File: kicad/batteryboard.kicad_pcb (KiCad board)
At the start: 2 copper layers, 41.9 x 72.4 mm, 19 parts, among them U1 PANSTAMP_02, U3 DHT22, U4 MAX1724

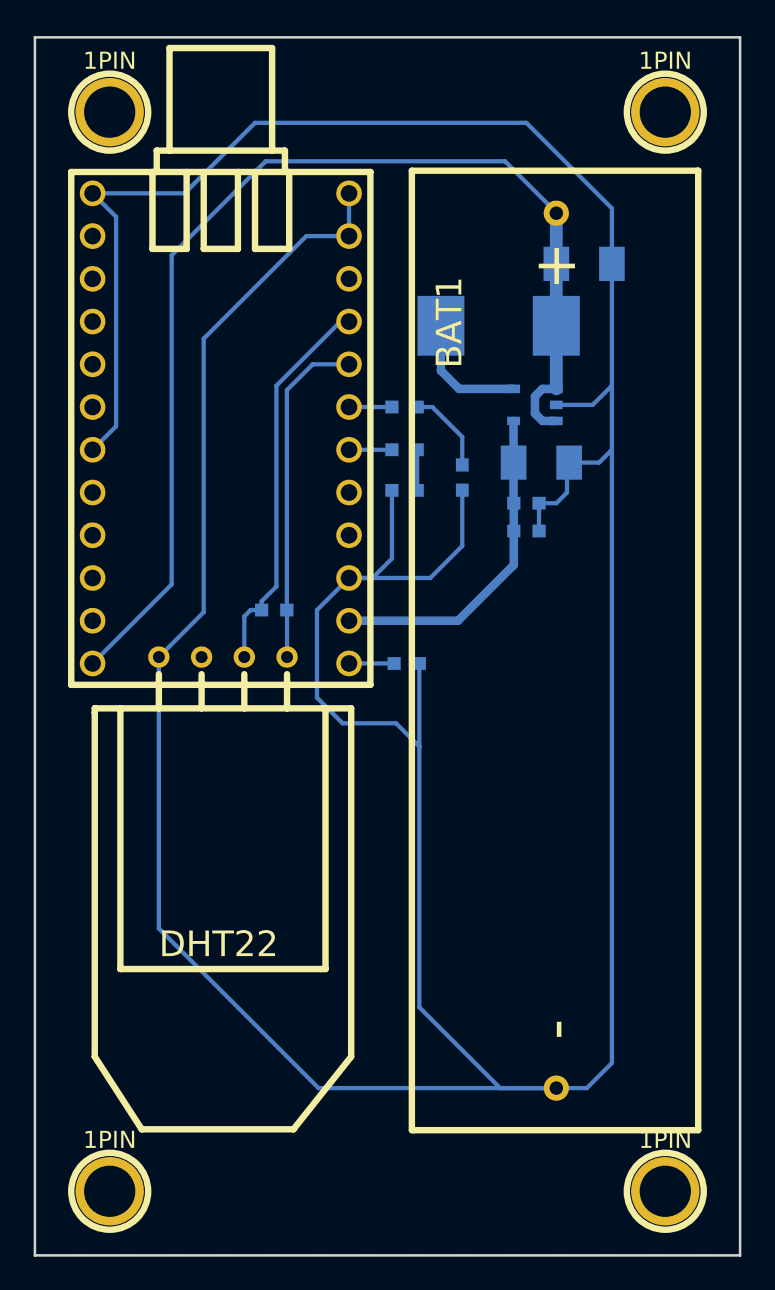
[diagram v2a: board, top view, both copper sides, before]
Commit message: add text
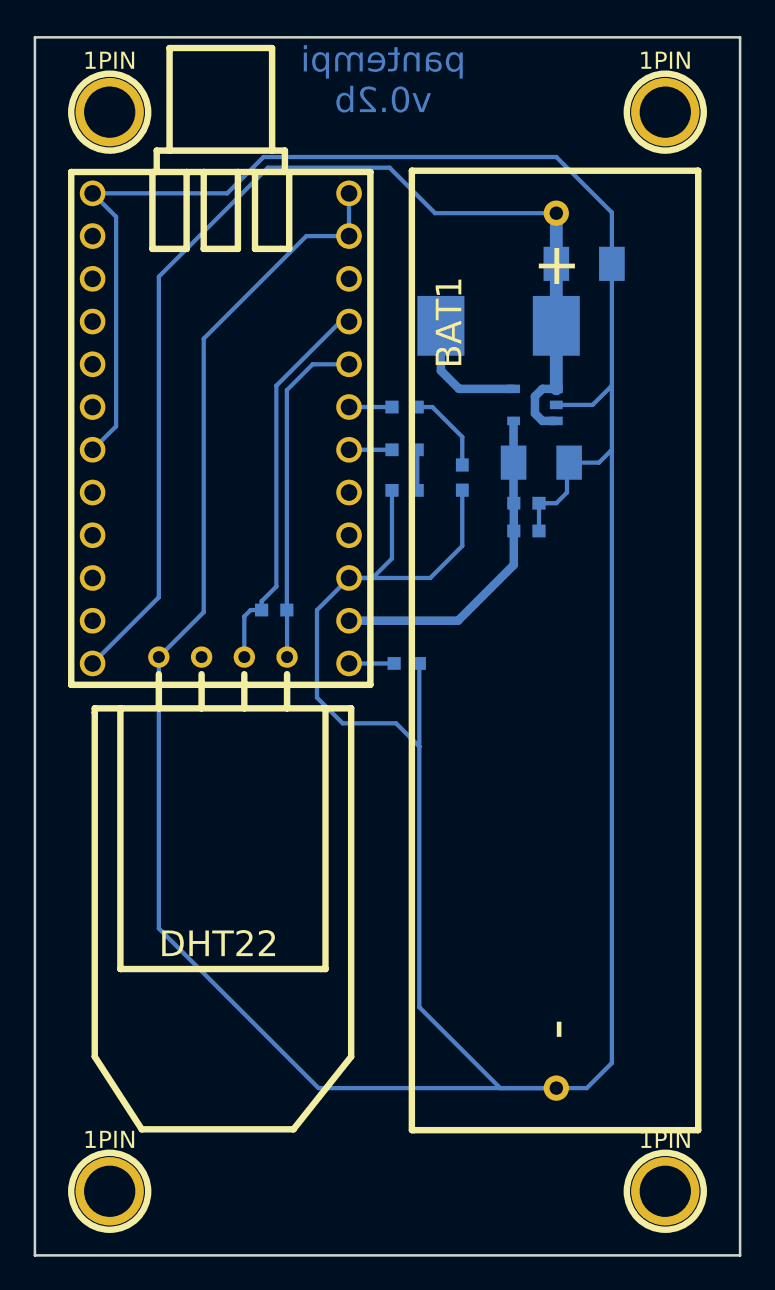
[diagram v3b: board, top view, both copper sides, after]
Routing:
- net GND: track 258.9 -> 257.1 mm
- net /BATTERY: track 67.0 -> 66.4 mm
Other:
- board text added: "pantempi v0.2b"
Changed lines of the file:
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@@
     (area 159.944999 68.504999 202.005001 141.045001)
     (thickness 1.6)
-    (drawings 4)
+    (drawings 5)
     (tracks 89)
     (zones 0)
@@
     )
   )
+  (gr_text "pantempi\nv0.2b" (at 180.721 71.12) (layer B.Cu)
+    (effects (font (size 1.5 1.5) (thickness 0.3)) (justify mirror))
+  )
   (gr_line (start 160.02 140.97) (end 160.02 68.58) (angle 90) (layer Edge.Cuts) (width 0.15))
   (gr_line (start 201.93 140.97) (end 160.02 140.97) (angle 90) (layer Edge.Cuts) (width 0.15))
@@
   (segment (start 188.468 96.2533) (end 188.4807 96.266) (width 0.508) (layer B.Cu) (net 1))
   (segment (start 188.468 91.3765) (end 188.468 93.853) (width 0.508) (layer B.Cu) (net 1))
-  (segment (start 173.4947 102.616) (end 173.4947 102.0953) (width 0.254) (layer B.Cu) (net 2) (status 400000))
-  (segment (start 178.181 85.471) (end 178.689 85.471) (width 0.254) (layer B.Cu) (net 2) (status C00000))
-  (segment (start 174.371 89.281) (end 178.181 85.471) (width 0.254) (layer B.Cu) (net 2) (status 800000))
+  (segment (start 173.4947 102.616) (end 173.4947 102.0953) (width 0.254) (layer B.Cu) (net 2))
+  (segment (start 178.181 85.471) (end 178.689 85.471) (width 0.254) (layer B.Cu) (net 2))
+  (segment (start 174.371 89.281) (end 178.181 85.471) (width 0.254) (layer B.Cu) (net 2))
   (segment (start 174.371 101.219) (end 174.371 89.281) (width 0.254) (layer B.Cu) (net 2))
   (segment (start 173.4947 102.0953) (end 174.371 101.219) (width 0.254) (layer B.Cu) (net 2))
-  (segment (start 172.466 105.41) (end 172.466 102.997) (width 0.254) (layer B.Cu) (net 2) (status 400000))
-  (segment (start 172.847 102.616) (end 173.4947 102.616) (width 0.254) (layer B.Cu) (net 2) (status 800000))
+  (segment (start 172.466 105.41) (end 172.466 102.997) (width 0.254) (layer B.Cu) (net 2))
+  (segment (start 172.847 102.616) (end 173.4947 102.616) (width 0.254) (layer B.Cu) (net 2))
   (segment (start 172.466 102.997) (end 172.847 102.616) (width 0.254) (layer B.Cu) (net 2))
-  (segment (start 174.9933 102.616) (end 174.9933 89.5477) (width 0.254) (layer B.Cu) (net 3) (status 400000))
-  (segment (start 176.53 88.011) (end 178.689 88.011) (width 0.254) (layer B.Cu) (net 3) (status 800000))
+  (segment (start 174.9933 102.616) (end 174.9933 89.5477) (width 0.254) (layer B.Cu) (net 3))
+  (segment (start 176.53 88.011) (end 178.689 88.011) (width 0.254) (layer B.Cu) (net 3))
   (segment (start 174.9933 89.5477) (end 176.53 88.011) (width 0.254) (layer B.Cu) (net 3))
-  (segment (start 175.006 105.41) (end 175.006 102.6287) (width 0.254) (layer B.Cu) (net 3) (status C00000))
-  (segment (start 175.006 102.6287) (end 174.9933 102.616) (width 0.254) (layer B.Cu) (net 3) (status C00000))
-  (segment (start 191.008 79.02956) (end 191.008 78.994) (width 0.254) (layer B.Cu) (net 4) (status C00000))
-  (segment (start 168.148 101.092) (end 163.449 105.791) (width 0.254) (layer B.Cu) (net 4) (status 800000))
-  (segment (start 168.148 81.534) (end 168.148 101.092) (width 0.254) (layer B.Cu) (net 4))
-  (segment (start 173.736 75.946) (end 168.148 81.534) (width 0.254) (layer B.Cu) (net 4))
-  (segment (start 187.96 75.946) (end 173.736 75.946) (width 0.254) (layer B.Cu) (net 4))
-  (segment (start 191.008 78.994) (end 187.96 75.946) (width 0.254) (layer B.Cu) (net 4) (status 400000))
+  (segment (start 175.006 105.41) (end 175.006 102.6287) (width 0.254) (layer B.Cu) (net 3))
+  (segment (start 175.006 102.6287) (end 174.9933 102.616) (width 0.254) (layer B.Cu) (net 3))
+  (segment (start 191.008 79.02956) (end 183.80456 79.02956) (width 0.254) (layer B.Cu) (net 4) (status 400000))
+  (segment (start 167.386 101.854) (end 163.449 105.791) (width 0.254) (layer B.Cu) (net 4) (status 800000))
+  (segment (start 167.386 82.804) (end 167.386 101.854) (width 0.254) (layer B.Cu) (net 4))
+  (segment (start 173.863 76.327) (end 167.386 82.804) (width 0.254) (layer B.Cu) (net 4))
+  (segment (start 181.102 76.327) (end 173.863 76.327) (width 0.254) (layer B.Cu) (net 4))
+  (segment (start 183.80456 79.02956) (end 181.102 76.327) (width 0.254) (layer B.Cu) (net 4))
   (segment (start 191.008 89.4715) (end 190.1825 89.4715) (width 0.508) (layer B.Cu) (net 4))
   (segment (start 190.1825 91.3765) (end 191.008 91.3765) (width 0.508) (layer B.Cu) (net 4))
@@
   (segment (start 181.2417 90.551) (end 178.689 90.551) (width 0.254) (layer B.Cu) (net 6))
   (segment (start 181.3687 105.791) (end 178.689 105.791) (width 0.254) (layer B.Cu) (net 7))
-  (segment (start 178.689 80.391) (end 176.149 80.391) (width 0.254) (layer B.Cu) (net 8) (status 400000))
-  (segment (start 170.053 102.743) (end 167.386 105.41) (width 0.254) (layer B.Cu) (net 8) (status 800000))
+  (segment (start 163.449 77.851) (end 171.45 77.851) (width 0.254) (layer B.Cu) (net 8) (status 400000))
+  (segment (start 194.31 78.994) (end 194.31 82.042) (width 0.254) (layer B.Cu) (net 8) (status 800000))
+  (segment (start 191.008 75.692) (end 194.31 78.994) (width 0.254) (layer B.Cu) (net 8))
+  (segment (start 173.609 75.692) (end 191.008 75.692) (width 0.254) (layer B.Cu) (net 8))
+  (segment (start 171.45 77.851) (end 173.609 75.692) (width 0.254) (layer B.Cu) (net 8))
+  (segment (start 178.689 80.391) (end 176.149 80.391) (width 0.254) (layer B.Cu) (net 8))
+  (segment (start 170.053 102.743) (end 167.386 105.41) (width 0.254) (layer B.Cu) (net 8))
   (segment (start 170.053 86.487) (end 170.053 102.743) (width 0.254) (layer B.Cu) (net 8))
   (segment (start 176.149 80.391) (end 170.053 86.487) (width 0.254) (layer B.Cu) (net 8))
-  (segment (start 163.449 77.851) (end 168.91 77.851) (width 0.254) (layer B.Cu) (net 8) (status 400000))
-  (segment (start 194.31 78.74) (end 194.31 82.042) (width 0.254) (layer B.Cu) (net 8) (status 800000))
-  (segment (start 189.23 73.66) (end 194.31 78.74) (width 0.254) (layer B.Cu) (net 8))
-  (segment (start 173.101 73.66) (end 189.23 73.66) (width 0.254) (layer B.Cu) (net 8))
-  (segment (start 168.91 77.851) (end 173.101 73.66) (width 0.254) (layer B.Cu) (net 8))
-  (segment (start 163.449 93.091) (end 164.846 91.694) (width 0.254) (layer B.Cu) (net 8) (status 400000))
-  (segment (start 164.846 79.248) (end 163.449 77.851) (width 0.254) (layer B.Cu) (net 8) (status 800000))
+  (segment (start 163.449 93.091) (end 164.846 91.694) (width 0.254) (layer B.Cu) (net 8))
+  (segment (start 164.846 79.248) (end 163.449 77.851) (width 0.254) (layer B.Cu) (net 8))
   (segment (start 164.846 91.694) (end 164.846 79.248) (width 0.254) (layer B.Cu) (net 8))
-  (segment (start 167.386 105.41) (end 167.386 121.539) (width 0.254) (layer B.Cu) (net 8) (status 400000))
+  (segment (start 167.386 105.41) (end 167.386 121.539) (width 0.254) (layer B.Cu) (net 8))
   (segment (start 167.386 121.539) (end 176.87544 131.02844) (width 0.254) (layer B.Cu) (net 8))
-  (segment (start 176.87544 131.02844) (end 191.008 131.02844) (width 0.254) (layer B.Cu) (net 8) (status 800000))
+  (segment (start 176.87544 131.02844) (end 191.008 131.02844) (width 0.254) (layer B.Cu) (net 8))
   (segment (start 185.42 95.4913) (end 185.42 98.806) (width 0.254) (layer B.Cu) (net 8))
   (segment (start 183.515 100.711) (end 178.689 100.711) (width 0.254) (layer B.Cu) (net 8))
